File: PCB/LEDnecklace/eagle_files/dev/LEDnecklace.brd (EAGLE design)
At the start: 35 x 35 mm, 6 parts, among them SW1 PCM12SMTR

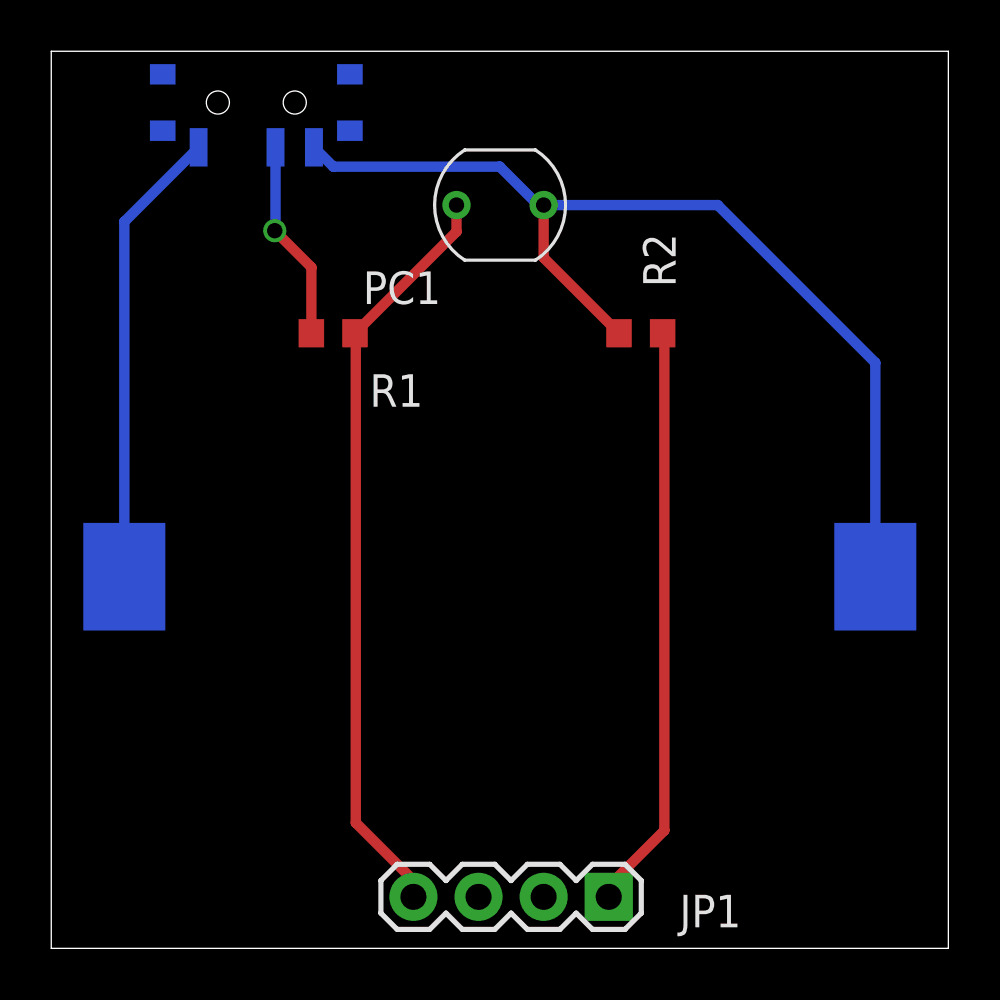
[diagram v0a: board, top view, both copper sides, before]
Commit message: Develop version of LEDnecklace with XLampXBD and smaller coin cell (type 2016).
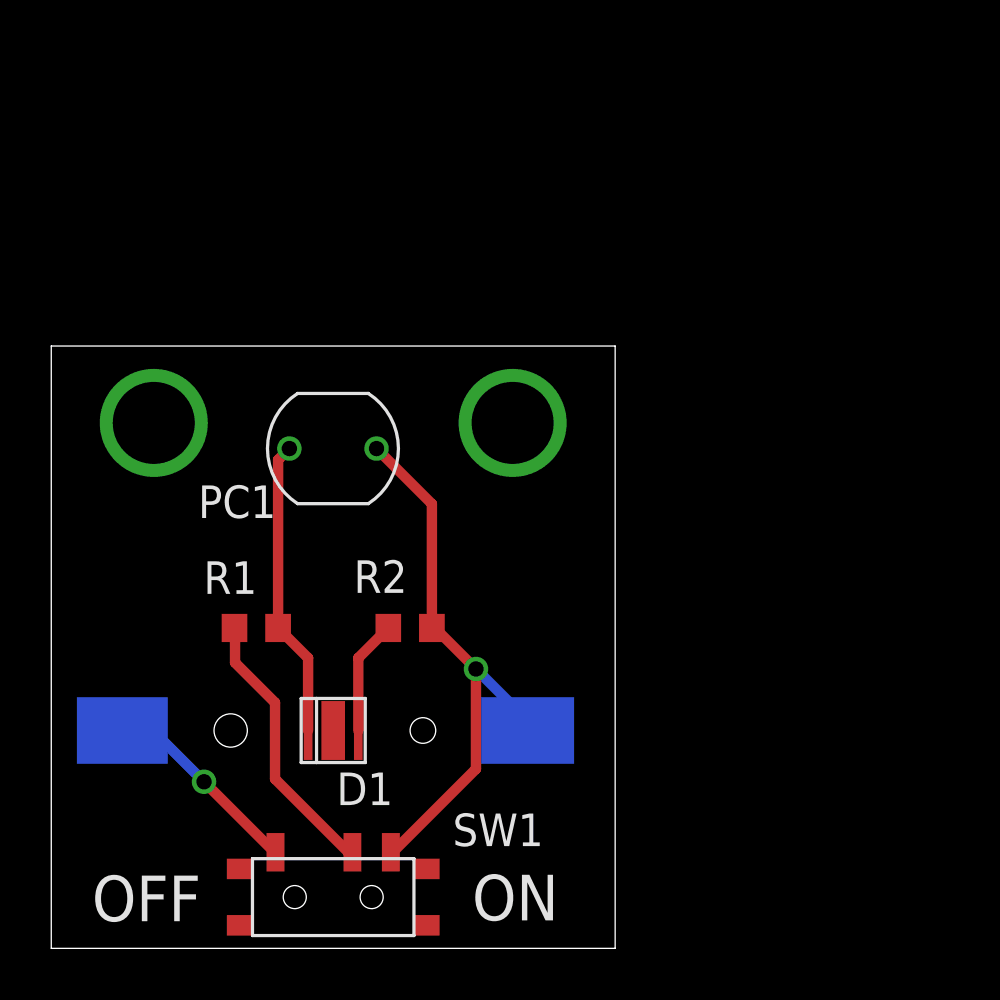
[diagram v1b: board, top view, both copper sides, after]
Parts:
- removed JP1: (no value), SparkFun-Connectors:1X04
- added D1: XLAMP_XBD, freddyLibr:XLAMP_XBD
- P1: value (none) -> BC501SM_BATT_HOLD; device freddyLibr:SMD_BATT_HOLDER_2032 -> freddyLibr:BC501SM_BATT_HOLD
- moved SW1 31.1 mm to (11.0, 2.00), flipped to the top, turned to 0 degrees
- moved R2 14.6 mm to (14.0, 12.5), turned to 180 degrees
- moved R1 11.9 mm to (8.00, 12.5)
- moved PC1 11.5 mm to (11.0, 19.5)
- moved P1 8.85 mm to (11.0, 8.50), turned to 0 degrees
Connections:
- removed net N$16: JP1.4, PC1.1, R1.1
- new net N$4: D1.AD, PC1.1, R1.1
- net N$5: now also D1.CD; no longer JP1.1
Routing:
- net N$16: track 29.6 -> 0.00 mm
- net N$5: track 22.9 -> 4.48 mm
- net N$2: track 39.9 -> 22.1 mm, vias 0 -> 1
- net N$4: track 0.00 -> 11.7 mm
- net N$3: track 18.0 -> 7.95 mm, vias 0 -> 1
- net N$1: track 7.85 -> 10.7 mm, vias 1 -> 0
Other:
- board size 35 x 35 mm -> 22 x 23.5 mm

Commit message: Change border around LED. Hopefully more visible.
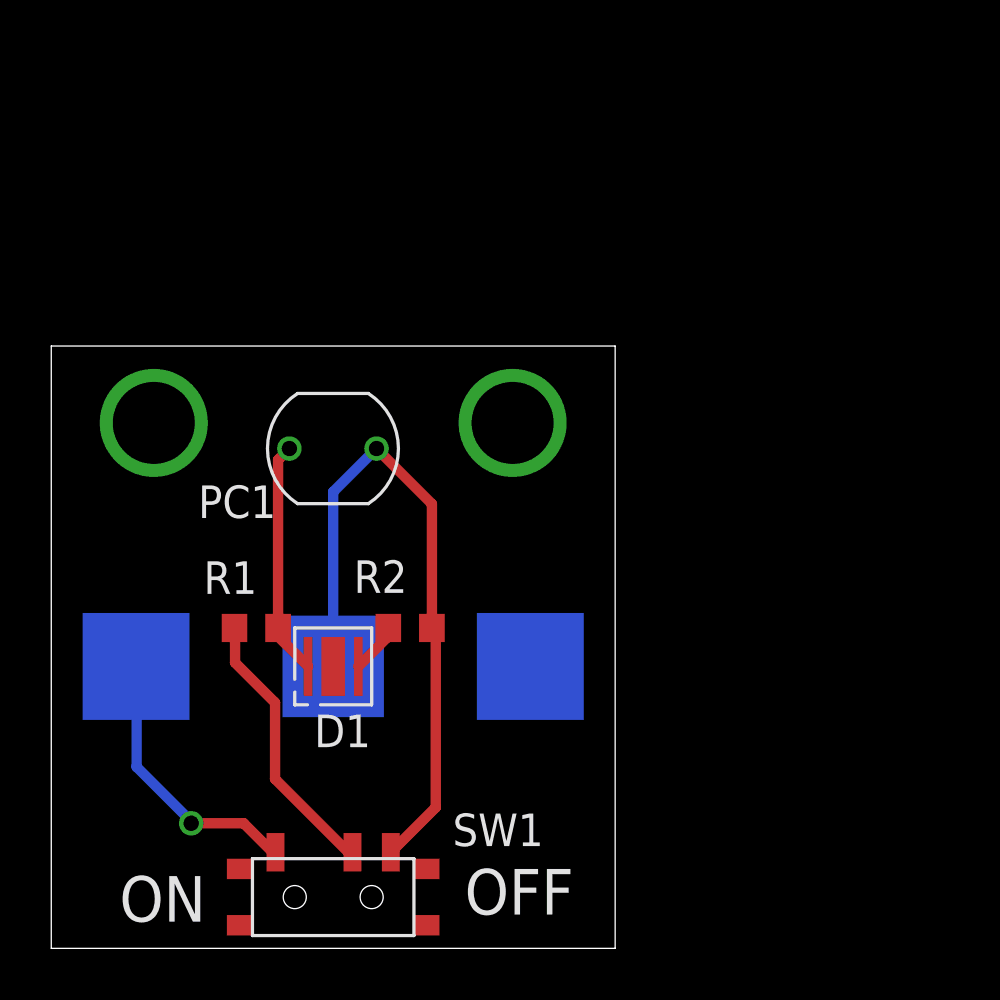
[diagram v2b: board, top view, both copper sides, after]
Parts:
- P1: value BC501SM_BATT_HOLD -> CR1220; device freddyLibr:BC501SM_BATT_HOLD -> freddyLibr:CR1220/1225
- moved D1 2.50 mm to (11.0, 11.0)
- moved P1 2.50 mm to (11.0, 11.0), turned to 180 degrees
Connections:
- net N$3: now also P1.VCC1; no longer P1.VCC
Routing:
- net N$2: track 22.1 -> 26.6 mm, vias 1 -> 0
- net N$3: track 7.95 -> 10.8 mm
- net N$4: track 11.7 -> 9.17 mm
- net N$5: track 4.48 -> 1.98 mm
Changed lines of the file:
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@@
 <wire x1="22" y1="23.5" x2="0" y2="23.5" width="0" layer="20"/>
 <wire x1="0" y1="23.5" x2="0" y2="0" width="0" layer="20"/>
-<text x="19.79" y="2.87" size="1.778" layer="21" rot="R180">ON</text>
-<text x="1.59" y="1.06" size="1.778" layer="21">OFF</text>
+<text x="6.03" y="2.82" size="1.778" layer="21" rot="R180">ON</text>
+<text x="16.13" y="1.32" size="1.778" layer="21">OFF</text>
 </plain>
 <attributes>
@@
 <attribute name="NAME" x="15.66" y="3.99" size="1.27" layer="25"/>
 </element>
-<element name="P1" library="freddyLibr" package="BC501SM_BATT_HOLD" value="BC501SM_BATT_HOLD" x="11" y="8.5" smashed="yes" rot="MR0">
-<attribute name="NAME" x="3.04" y="11.15" size="1.27" layer="26" rot="MR0"/>
-</element>
-<element name="D1" library="freddyLibr" package="XLAMP_XBD" value="XLAMP_XBD" x="11" y="8.5" smashed="yes">
-<attribute name="NAME" x="11.13" y="5.59" size="1.27" layer="25"/>
+<element name="P1" library="freddyLibr" package="CR1220/1225" value="CR1220" x="11" y="11" smashed="yes" rot="MR180">
+<attribute name="NAME" x="18.45" y="8.2" size="1.27" layer="26" rot="MR180"/>
+</element>
+<element name="D1" library="freddyLibr" package="XLAMP_XBD" value="XLAMP_XBD" x="11" y="11" smashed="yes">
+<attribute name="NAME" x="10.26" y="7.85" size="1.27" layer="25"/>
 </element>
 </elements>
@@
 <contactref element="PC1" pad="2"/>
 <contactref element="SW1" pad="3"/>
-<contactref element="P1" pad="GND"/>
-<wire x1="14.85" y1="12.5" x2="14.97" y2="12.5" width="0.4064" layer="1"/>
-<wire x1="14.97" y1="12.5" x2="16.57" y2="10.9" width="0.4064" layer="1"/>
-<via x="16.57" y="10.9" extent="1-16" drill="0.6"/>
-<wire x1="16.57" y1="10.9" x2="18.24" y2="9.23" width="0.4064" layer="16"/>
-<wire x1="18.24" y1="9.23" x2="18.24" y2="8.83" width="0.4064" layer="16"/>
-<wire x1="18.24" y1="8.83" x2="18.57" y2="8.5" width="0.4064" layer="16"/>
 <wire x1="14.85" y1="12.5" x2="14.85" y2="17.34" width="0.4064" layer="1"/>
 <wire x1="14.85" y1="17.34" x2="12.69" y2="19.5" width="0.4064" layer="1"/>
-<wire x1="13.25" y1="3.75" x2="13.32" y2="3.75" width="0.4064" layer="1"/>
-<wire x1="13.32" y1="3.75" x2="16.57" y2="7" width="0.4064" layer="1"/>
-<wire x1="16.57" y1="7" x2="16.57" y2="10.9" width="0.4064" layer="1"/>
+<contactref element="P1" pad="GND"/>
+<wire x1="13.25" y1="3.75" x2="15" y2="5.5" width="0.4064" layer="1"/>
+<wire x1="15" y1="5.5" x2="15" y2="12.35" width="0.4064" layer="1"/>
+<wire x1="15" y1="12.35" x2="14.85" y2="12.5" width="0.4064" layer="1"/>
+<wire x1="11" y1="11" x2="11" y2="17.81" width="0.4064" layer="16"/>
+<wire x1="11" y1="17.81" x2="12.69" y2="19.5" width="0.4064" layer="16"/>
 </signal>
 <signal name="N$1">
@@
 <signal name="N$3">
 <contactref element="SW1" pad="1"/>
-<contactref element="P1" pad="VCC"/>
-<wire x1="8.75" y1="3.75" x2="8.71" y2="3.75" width="0.4064" layer="1"/>
-<wire x1="8.71" y1="3.75" x2="5.96" y2="6.5" width="0.4064" layer="1"/>
-<via x="5.96" y="6.5" extent="1-16" drill="0.6"/>
-<wire x1="5.96" y1="6.5" x2="4.01" y2="8.45" width="0.4064" layer="16"/>
-<wire x1="4.01" y1="8.45" x2="2.82" y2="8.45" width="0.4064" layer="16"/>
-<wire x1="2.82" y1="8.45" x2="2.77" y2="8.5" width="0.4064" layer="16"/>
+<contactref element="P1" pad="VCC1"/>
+<wire x1="8.75" y1="3.75" x2="8.64" y2="3.75" width="0.4064" layer="1"/>
+<wire x1="8.64" y1="3.75" x2="7.51" y2="4.88" width="0.4064" layer="1"/>
+<wire x1="7.51" y1="4.88" x2="5.46" y2="4.88" width="0.4064" layer="1"/>
+<via x="5.46" y="4.88" extent="1-16" drill="0.6"/>
+<wire x1="5.46" y1="4.88" x2="5.46" y2="4.95" width="0.4064" layer="16"/>
+<wire x1="5.46" y1="4.95" x2="3.33" y2="7.08" width="0.4064" layer="16"/>
+<wire x1="3.33" y1="7.08" x2="3.33" y2="10.98" width="0.4064" layer="16"/>
+<wire x1="3.33" y1="10.98" x2="3.31" y2="11" width="0.4064" layer="16"/>
 </signal>
 <signal name="N$4">
 <contactref element="R1" pad="1"/>
 <contactref element="PC1" pad="1"/>
-<contactref element="D1" pad="AD"/>
-<wire x1="10.02" y1="8.5" x2="10.02" y2="11.33" width="0.4064" layer="1"/>
-<wire x1="10.02" y1="11.33" x2="8.85" y2="12.5" width="0.4064" layer="1"/>
 <wire x1="8.85" y1="12.5" x2="8.85" y2="19.06" width="0.4064" layer="1"/>
 <wire x1="8.85" y1="19.06" x2="9.29" y2="19.5" width="0.4064" layer="1"/>
+<contactref element="D1" pad="AD"/>
+<wire x1="8.85" y1="12.5" x2="8.85" y2="12.17" width="0.4064" layer="1"/>
+<wire x1="8.85" y1="12.17" x2="10.02" y2="11" width="0.4064" layer="1"/>
 </signal>
 <signal name="N$5">
 <contactref element="R2" pad="2"/>
 <contactref element="D1" pad="CD"/>
-<wire x1="11.98" y1="8.5" x2="11.98" y2="11.33" width="0.4064" layer="1"/>
-<wire x1="11.98" y1="11.33" x2="13.15" y2="12.5" width="0.4064" layer="1"/>
+<wire x1="13.15" y1="12.5" x2="13.15" y2="12.17" width="0.4064" layer="1"/>
+<wire x1="13.15" y1="12.17" x2="11.98" y2="11" width="0.4064" layer="1"/>
 </signal>
 <signal name="N$6">
@@
 <via x="18" y="20.5" extent="1-16" drill="3.2"/>
 </signal>
+<signal name="N$8">
+</signal>
 </signals>
